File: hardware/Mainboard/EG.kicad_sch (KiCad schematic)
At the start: 27 parts, among them J11 Jumper, Q10 2N3904, Q13 2N3904, Q15 2N3904, Q2 2N3904, SW2 SW_SPST, U5 TL074

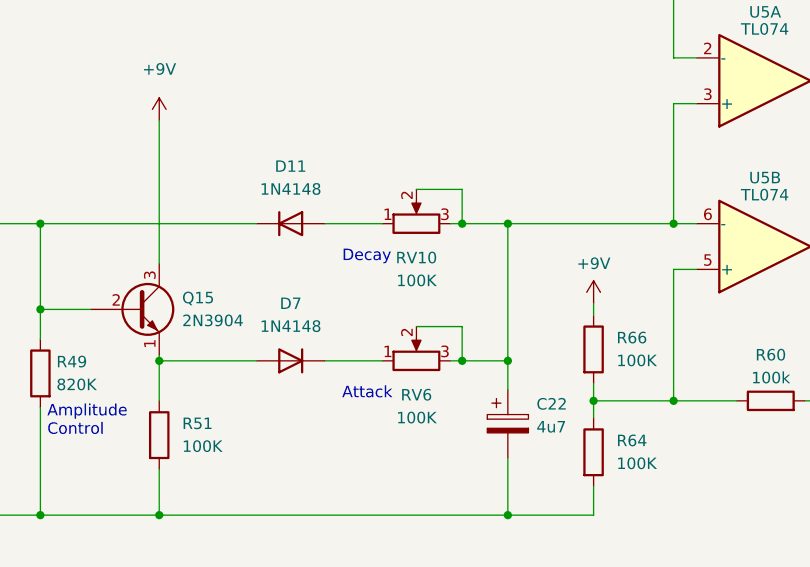
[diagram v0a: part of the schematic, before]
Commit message: Rename Decay -> Release
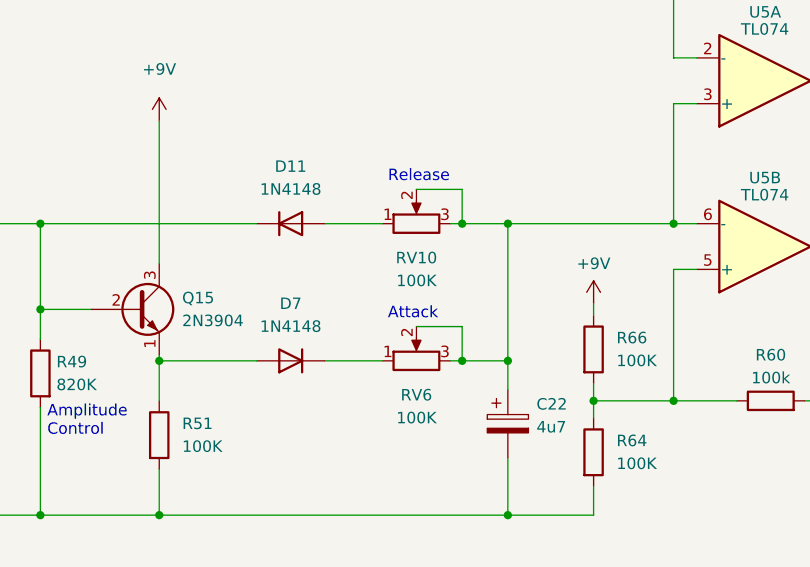
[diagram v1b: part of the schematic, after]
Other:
- note added: "Release"
- note removed: "Decay"
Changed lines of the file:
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@@
     (effects (font (size 1.27 1.27)) (justify left bottom))
   )
-  (text "Attack" (at 154.94 107.95 0)
+  (text "Attack" (at 160.02 99.06 0)
     (effects (font (size 1.27 1.27)) (justify left bottom))
   )
@@
     (effects (font (size 1.27 1.27)) (justify left bottom))
   )
-  (text "Decay" (at 154.94 92.71 0)
+  (text "Release" (at 160.02 83.82 0)
     (effects (font (size 1.27 1.27)) (justify left bottom))
   )
